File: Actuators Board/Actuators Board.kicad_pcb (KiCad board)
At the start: 2 copper layers, 97 parts, among them IC1 BD62120AEFJ-E2, J10 Conn_01x02_Male, J3 USB_C_Receptacle_USB2.0, J4 Conn_01x03_Male, J5 Conn_01x06_Male, J9 Conn_01x02_Male, Q1 MMDT2222A, Q2 SI2366DS, U1 ESP32-PICO-D4, U2 TPS54233D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

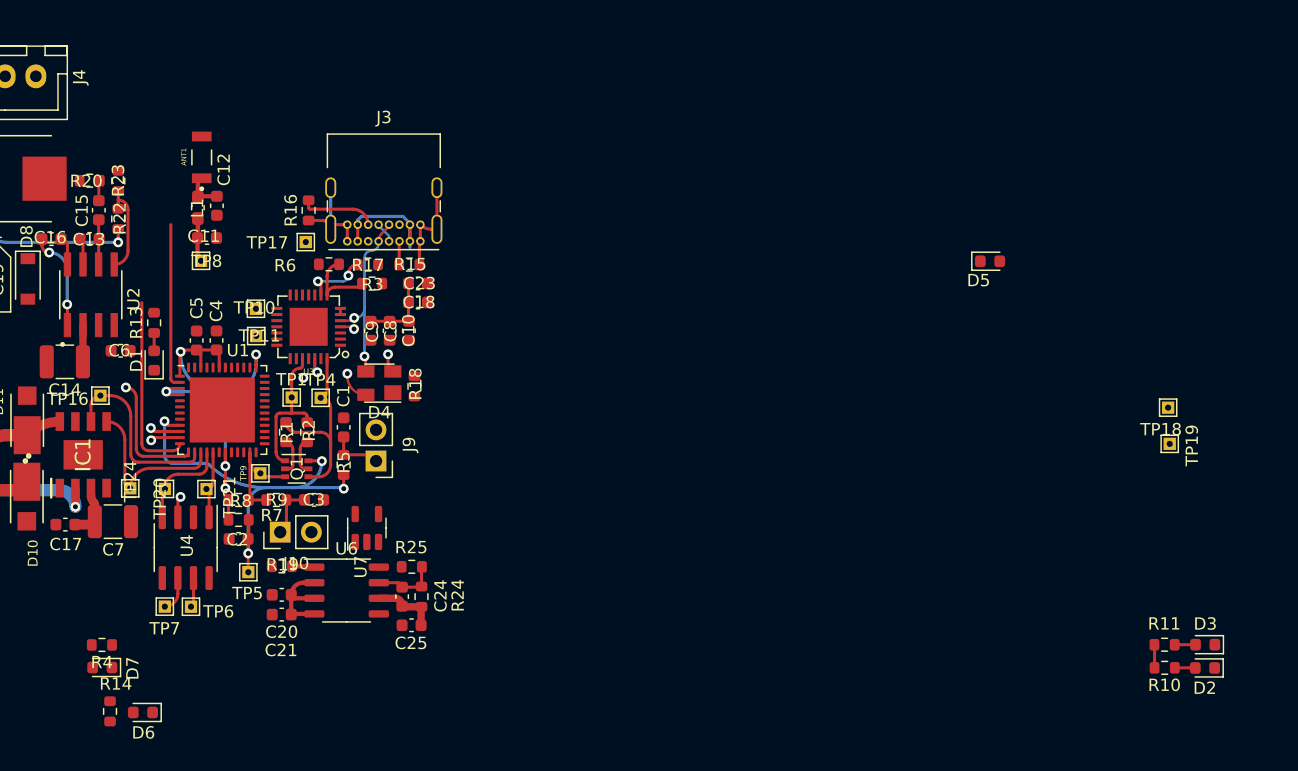
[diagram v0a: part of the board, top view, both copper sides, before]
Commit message: Connected usb & uart to esp32
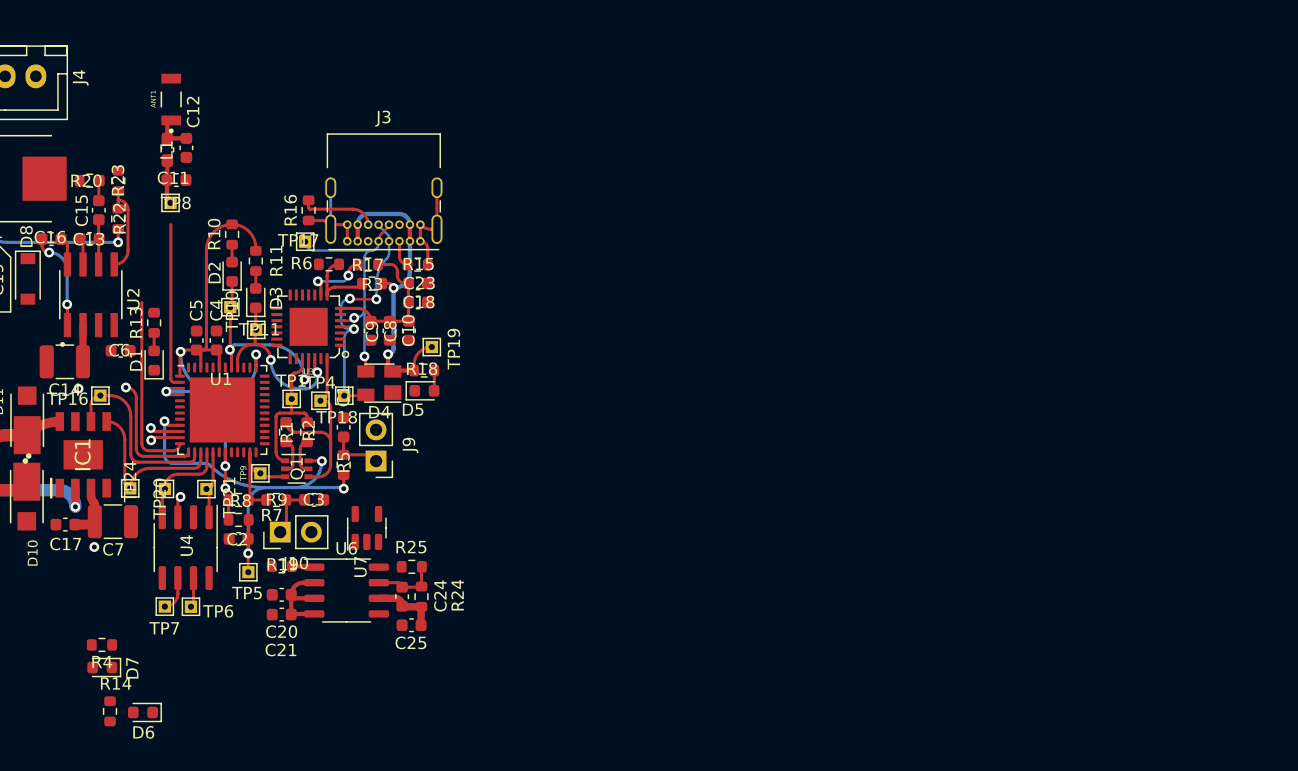
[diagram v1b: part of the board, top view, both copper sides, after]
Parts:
- moved D2 85.5 mm to (161.1, 95.1), turned to 90 degrees
- moved R10 83.7 mm to (161.1, 92.1), turned to -90 degrees
- moved D3 82.3 mm to (163.1, 97.3), turned to 90 degrees
- moved R11 80.3 mm to (163.1, 94.2), turned to -90 degrees
- moved TP18 67.1 mm to (170.3, 105.2)
- moved TP19 60.6 mm to (177.4, 101.3)
- moved D5 47.2 mm to (176.8, 104.8)
- moved TP8 5.33 mm to (156.1, 89.5)
- moved C12 5.33 mm to (157.4, 85.0)
- moved ANT1 5.33 mm to (156.2, 81.1)
- moved C11 5.33 mm to (156.6, 87.7)
- moved L1 5.33 mm to (155.9, 85.2)
- moved TP10 2.09 mm to (161.0, 98.0)
- moved R18 1.51 mm to (176.8, 103.2), turned to 0 degrees
- moved R15 0.68 mm to (176.2, 94.5)
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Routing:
- net +3V3: track 48.4 -> 67.6 mm
- net /RXD: track 0.00 -> 16.9 mm, vias 0 -> 2
- net /USB -> UART/Data+: track 5.50 -> 21.3 mm, vias 1 -> 3
- net VBUS: track 19.8 -> 35.4 mm, vias 1 -> 2
- net /TXD: track 1.22 -> 14.9 mm, vias 0 -> 2
- net /USB -> UART/Data-: track 15.5 -> 21.3 mm, vias 1 -> 2
- net Net-(D5-Pad2): track 0.00 -> 1.66 mm
- net +24V: vias 0 -> 2
- net (no net): vias 4 -> 0

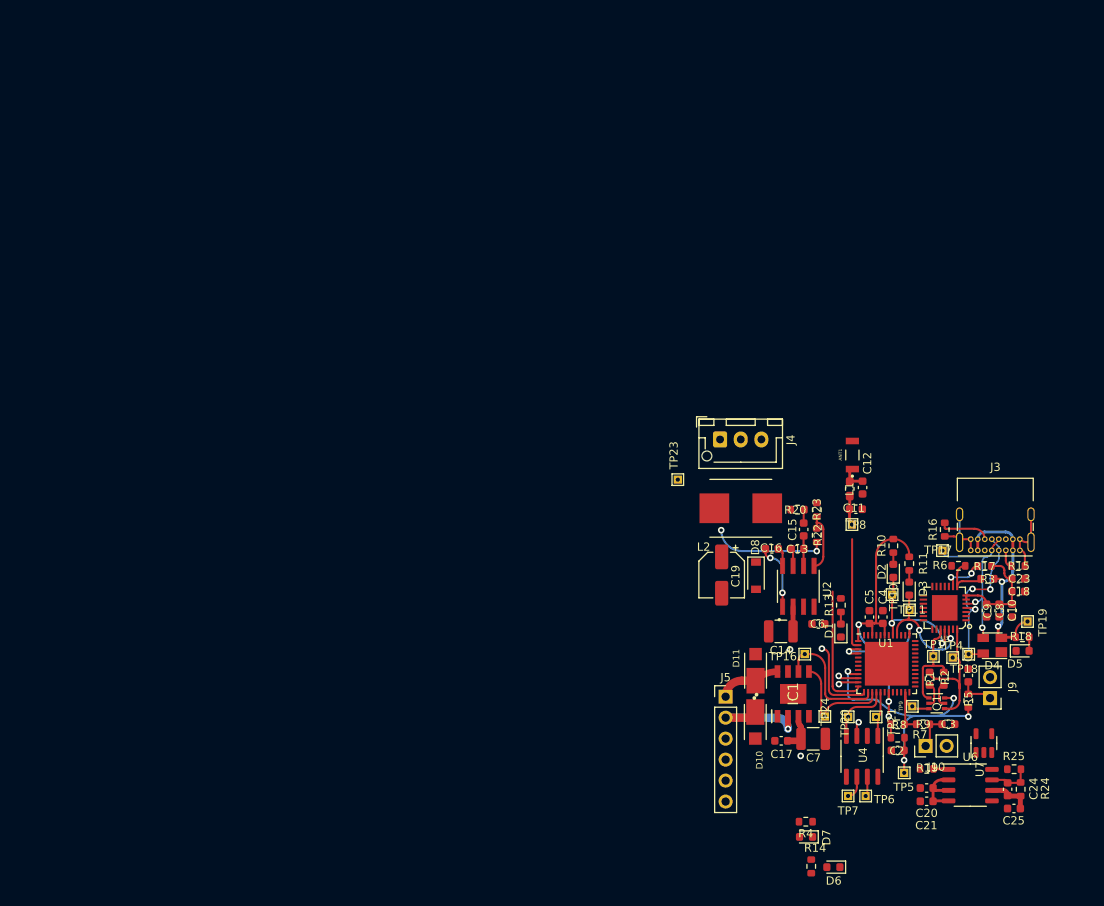
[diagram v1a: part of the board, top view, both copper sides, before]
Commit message: Added mounting holes, initial placement inside 50x50 board
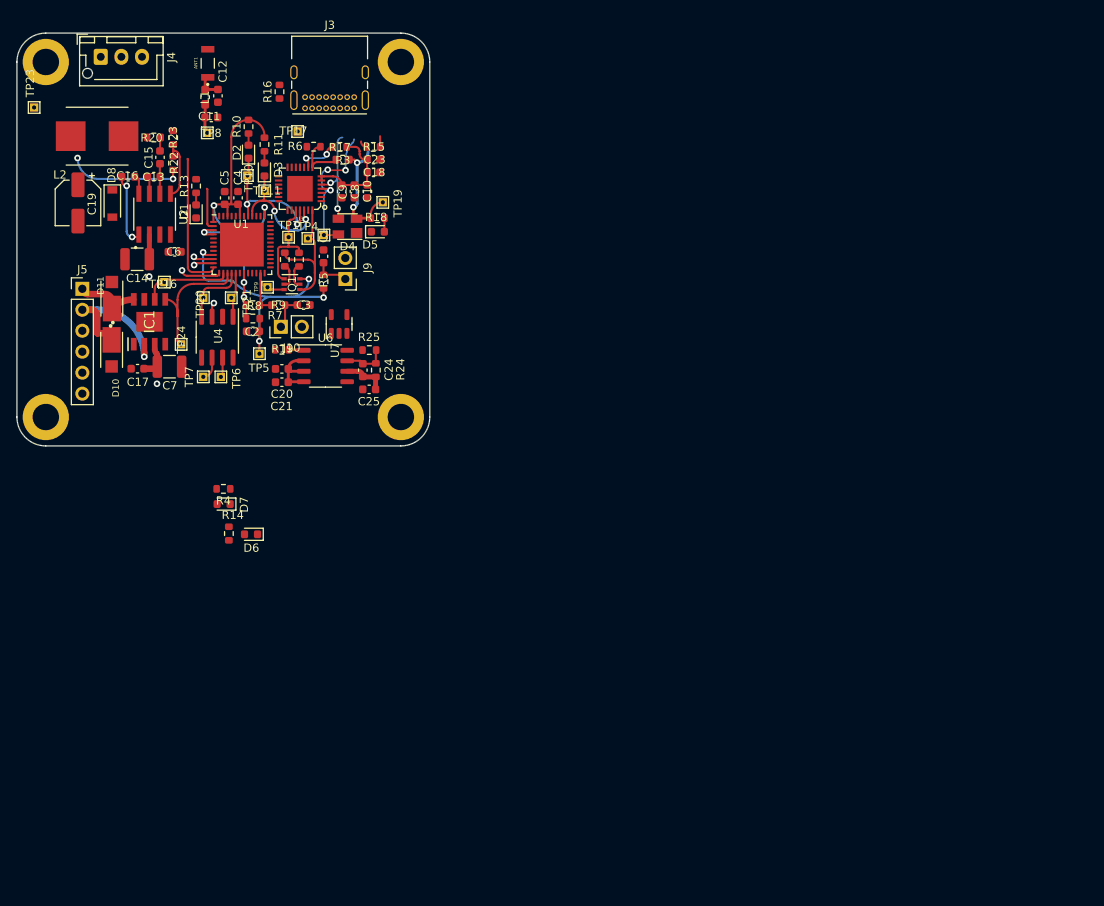
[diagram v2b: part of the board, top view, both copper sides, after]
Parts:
- added H1: MountingHole_Pad, MountingHole:MountingHole_3.2mm_M3_DIN965_Pad, F.Cu at (58.5, 76.5)
- added H2: MountingHole_Pad, MountingHole:MountingHole_3.2mm_M3_DIN965_Pad, F.Cu at (101.5, 33.5)
- added H3: MountingHole_Pad, MountingHole:MountingHole_3.2mm_M3_DIN965_Pad, F.Cu at (101.5, 76.5)
- added H4: MountingHole_Pad, MountingHole:MountingHole_3.2mm_M3_DIN965_Pad, F.Cu at (58.5, 33.5)
- moved J3 96.8 mm to (95.8, 39.1)
- moved R16 96.5 mm to (86.8, 37.1)
- moved C18 93.1 mm to (98.2, 46.9)
- moved J9 93.1 mm to (94.8, 59.8)
- moved R3 93.1 mm to (94.4, 45.3)
- moved U4 93.1 mm to (79.3, 66.8)
- moved C1 93.1 mm to (92.1, 57.0)
- moved C10 93.1 mm to (97.4, 49.2)
- moved C20 93.1 mm to (87.1, 70.7)
- moved C21 93.1 mm to (87.1, 72.3)
- moved C23 93.1 mm to (98.2, 45.3)
- moved C25 93.1 mm to (97.7, 73.2)
- moved C3 93.1 mm to (89.7, 62.9)
- moved C4 93.1 mm to (81.8, 50.0)
- moved C5 93.1 mm to (80.2, 50.0)
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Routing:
- net GND: track 19.7 -> 3.50 mm
- net VBUS: track 35.4 -> 23.4 mm
- net /USB -> UART/Data-: track 21.3 -> 12.8 mm
- net /LNA_IN: track 17.1 -> 8.80 mm
- net Net-(J3-PadB5): track 6.20 -> 0.00 mm
- net /Motor-: track 13.7 -> 19.5 mm
- net /ServoPWM: track 10.2 -> 5.02 mm
- net /HBridgeDIR2: track 15.2 -> 10.4 mm
- net /USB -> UART/Data+: track 21.3 -> 18.6 mm
- net /HBridgeDIR1: track 14.1 -> 16.6 mm
- net Net-(J3-PadA5): track 2.28 -> 1.01 mm
- net /SolEN: track 15.6 -> 16.9 mm
- net Net-(C16-Pad1): track 8.10 -> 8.93 mm
- net /Motor+: track 7.59 -> 8.20 mm
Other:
- board outline added: 50 x 50 mm

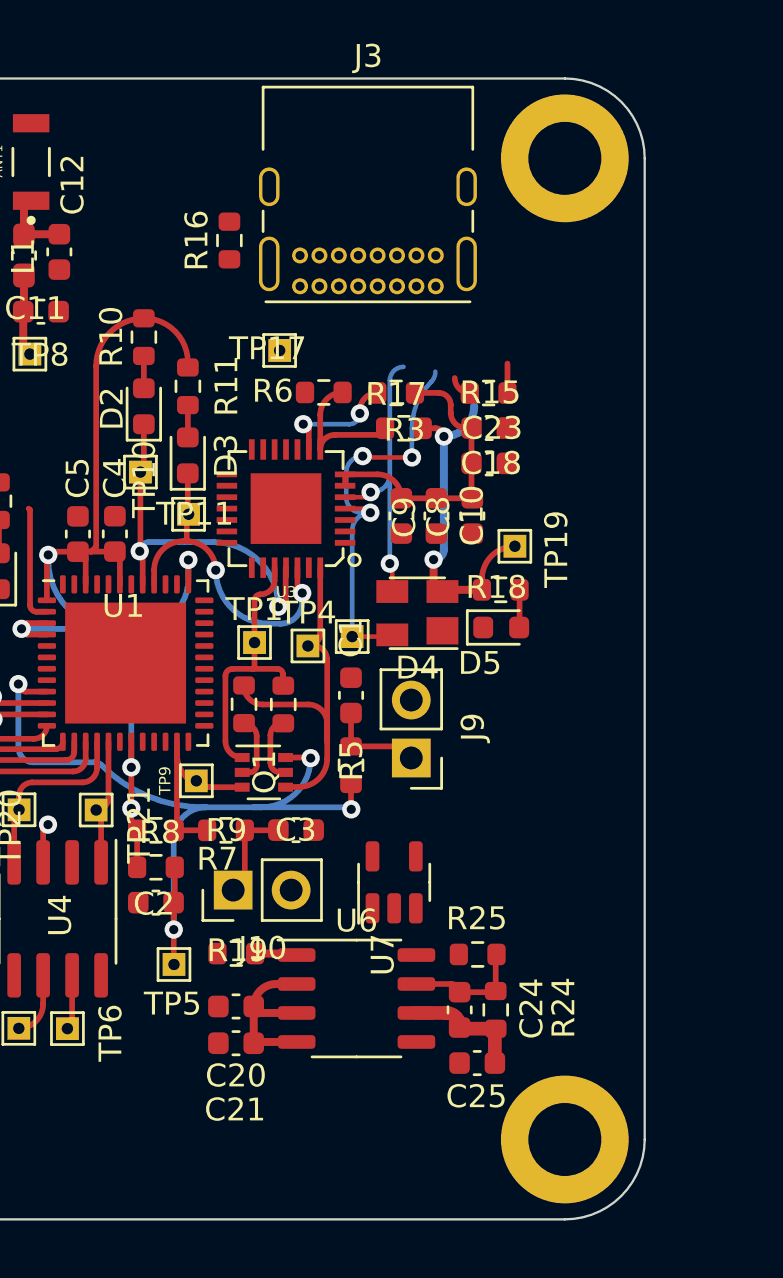
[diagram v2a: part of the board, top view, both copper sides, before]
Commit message: Provisional layout of USB supporting components
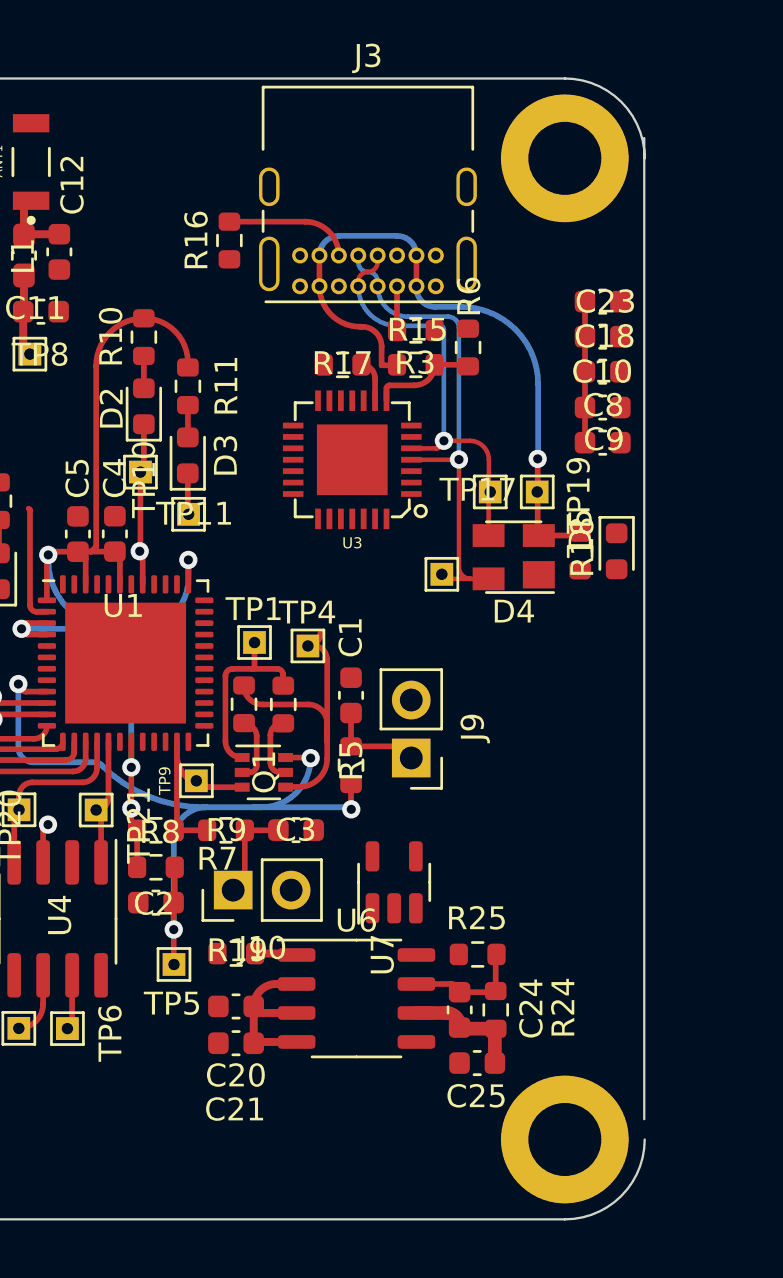
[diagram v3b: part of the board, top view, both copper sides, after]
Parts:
- moved TP17 11.1 mm to (98.2, 48.1)
- moved C9 9.39 mm to (103.2, 46.0), turned to 180 degrees
- moved C8 8.70 mm to (103.2, 44.4), turned to 180 degrees
- moved C10 8.52 mm to (103.2, 42.9), turned to 180 degrees
- moved C18 7.46 mm to (103.2, 41.3)
- moved C23 7.44 mm to (103.2, 39.8)
- moved R6 6.62 mm to (97.3, 41.8), turned to -90 degrees
- moved D5 6.06 mm to (103.8, 50.7), turned to -90 degrees
- moved D4 4.88 mm to (99.3, 51.0)
- moved TP18 4.79 mm to (96.1, 51.7)
- moved R15 4.21 mm to (95.0, 41.0)
- moved R18 3.86 mm to (102.2, 50.7), turned to -90 degrees
- moved U3 3.61 mm to (92.2, 46.7)
- moved R3 2.83 mm to (95.0, 42.5), turned to 0 degrees
- moved R17 2.65 mm to (91.8, 42.5), turned to 0 degrees
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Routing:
- net VBUS: track 23.4 -> 37.7 mm, vias 2 -> 1
- net /TXD: track 14.9 -> 1.94 mm, vias 2 -> 0
- net /RXD: track 16.9 -> 7.18 mm, vias 2 -> 1
- net +3V3: track 67.6 -> 60.7 mm
- net /USB -> UART/Data-: track 12.8 -> 19.0 mm, vias 2 -> 1
- net Net-(J3-PadB5): track 0.00 -> 5.58 mm
- net /RTS: track 12.2 -> 8.47 mm
- net Net-(R17-Pad2): track 5.58 -> 1.89 mm, vias 2 -> 0
- net /USB -> UART/Data+: track 18.6 -> 21.6 mm, vias 3 -> 1
- net /DTR: track 17.1 -> 14.2 mm
- net Net-(R3-Pad2): track 6.46 -> 4.69 mm
- net Net-(D5-Pad2): track 1.66 -> 0.00 mm
- net GND: track 3.50 -> 2.21 mm
- net Net-(J3-PadA5): track 1.01 -> 1.93 mm
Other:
- outline, holes or cut-outs redrawn

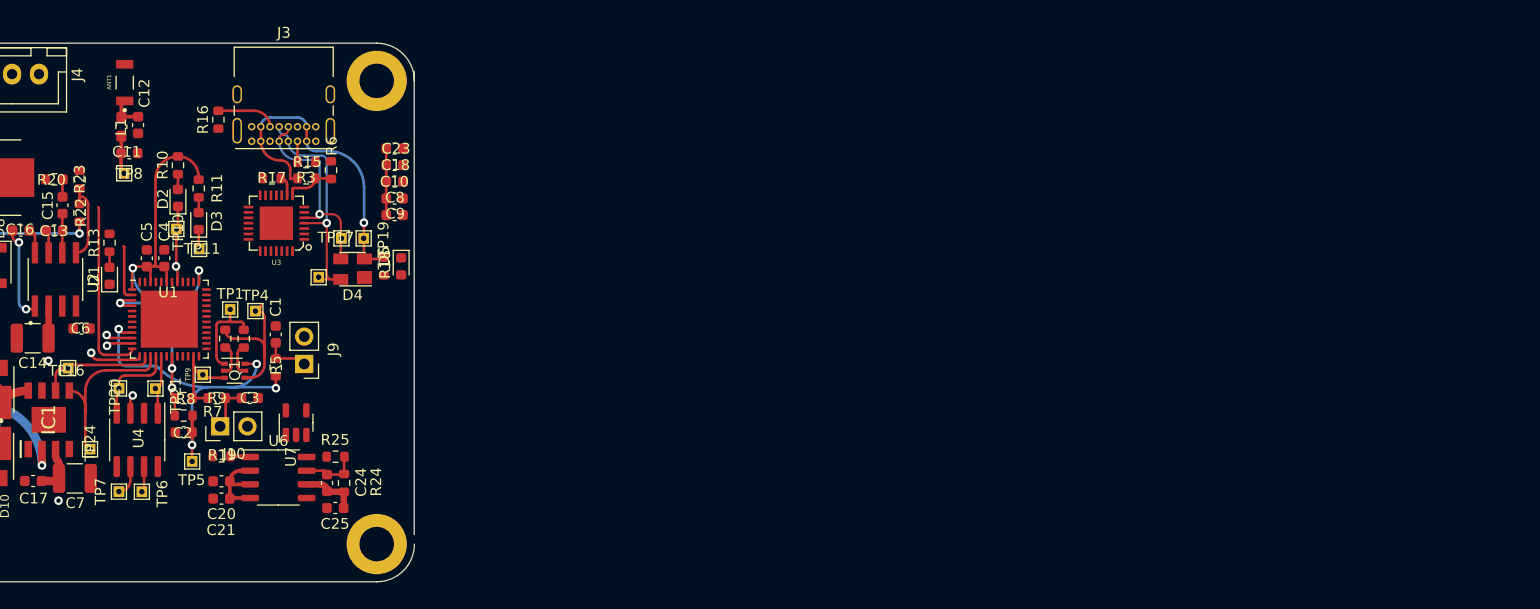
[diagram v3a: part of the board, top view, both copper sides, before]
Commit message: More USB connections, placement of 3.3V regulator
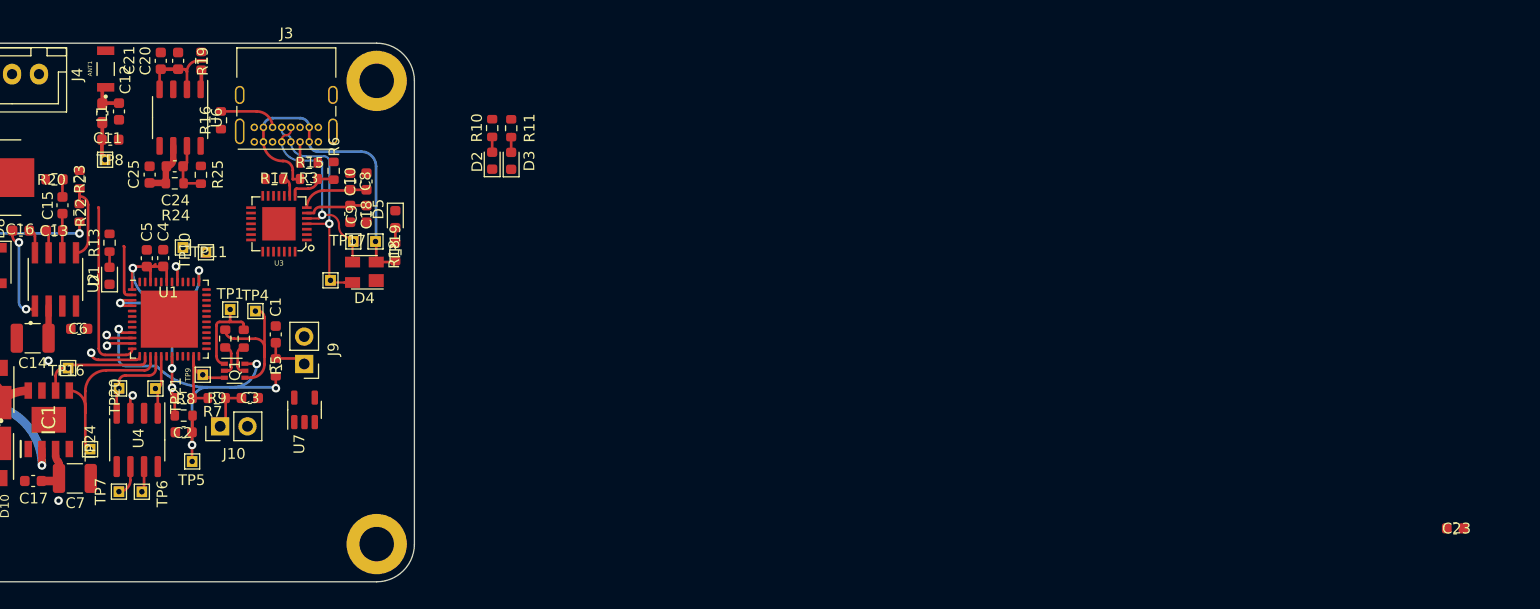
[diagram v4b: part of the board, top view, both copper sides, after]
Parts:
- moved C23 104.6 mm to (201.6, 75.0)
- moved C21 41.0 mm to (81.5, 31.6), turned to -90 degrees
- moved C20 39.2 mm to (83.1, 31.6), turned to -90 degrees
- moved R19 36.8 mm to (85.2, 31.6), turned to 90 degrees
- moved C25 35.4 mm to (80.4, 42.2), turned to -90 degrees
- moved U6 34.6 mm to (83.2, 36.9), turned to -90 degrees
- moved C24 32.6 mm to (82.8, 41.4), turned to 180 degrees
- moved R24 31.9 mm to (82.8, 43.0), turned to 0 degrees
- moved D3 29.5 mm to (114.0, 40.9)
- moved R11 29.5 mm to (114.0, 37.9)
- moved D2 29.4 mm to (112.2, 40.9)
- moved R10 29.4 mm to (112.2, 37.9)
- moved R25 29.0 mm to (85.2, 42.2), turned to 90 degrees
- moved C18 5.23 mm to (100.5, 45.8), turned to 90 degrees
- moved D5 4.41 mm to (103.2, 46.3)
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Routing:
- net +3V3: track 60.7 -> 52.5 mm
- net /RXD: track 7.18 -> 1.56 mm
- net VBUS: track 37.7 -> 40.1 mm, vias 1 -> 0
- net /TXD: track 1.94 -> 0.00 mm
- net Net-(D5-Pad2): track 0.00 -> 1.45 mm
- net /DTR: track 14.2 -> 13.3 mm
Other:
- outline, holes or cut-outs redrawn
